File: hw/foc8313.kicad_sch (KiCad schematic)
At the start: 78 parts, among them J1 Tag Connect, J2 Encoder, J3 CAN, J4 CAN, J6 GPIO, SW1 SW_SPST, SW2 SW_SPST, U1 LMR36015SFBRNXR, U2 XC6206P332MR, U3 DRV8313PWP, U4 STM32F103CBTx, U5 AS5047D, X1 X322516MLB4SI

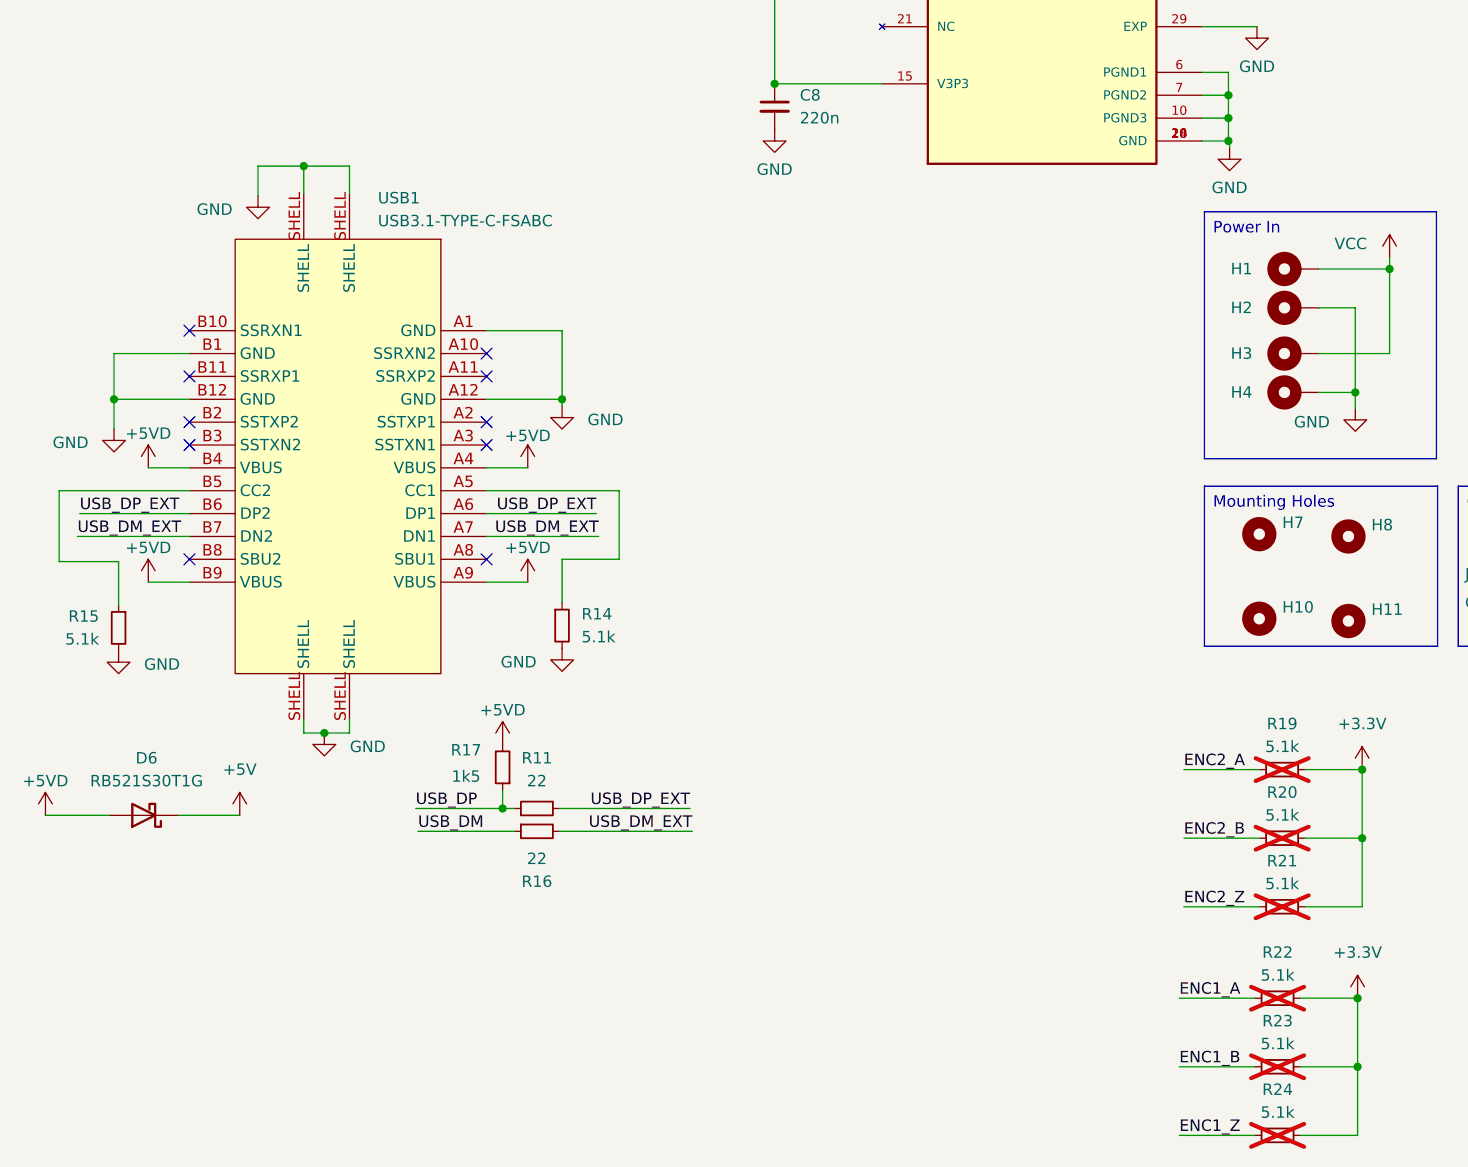
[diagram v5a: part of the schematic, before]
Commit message: [Hw]  LCSC versions of isolated CAN parts
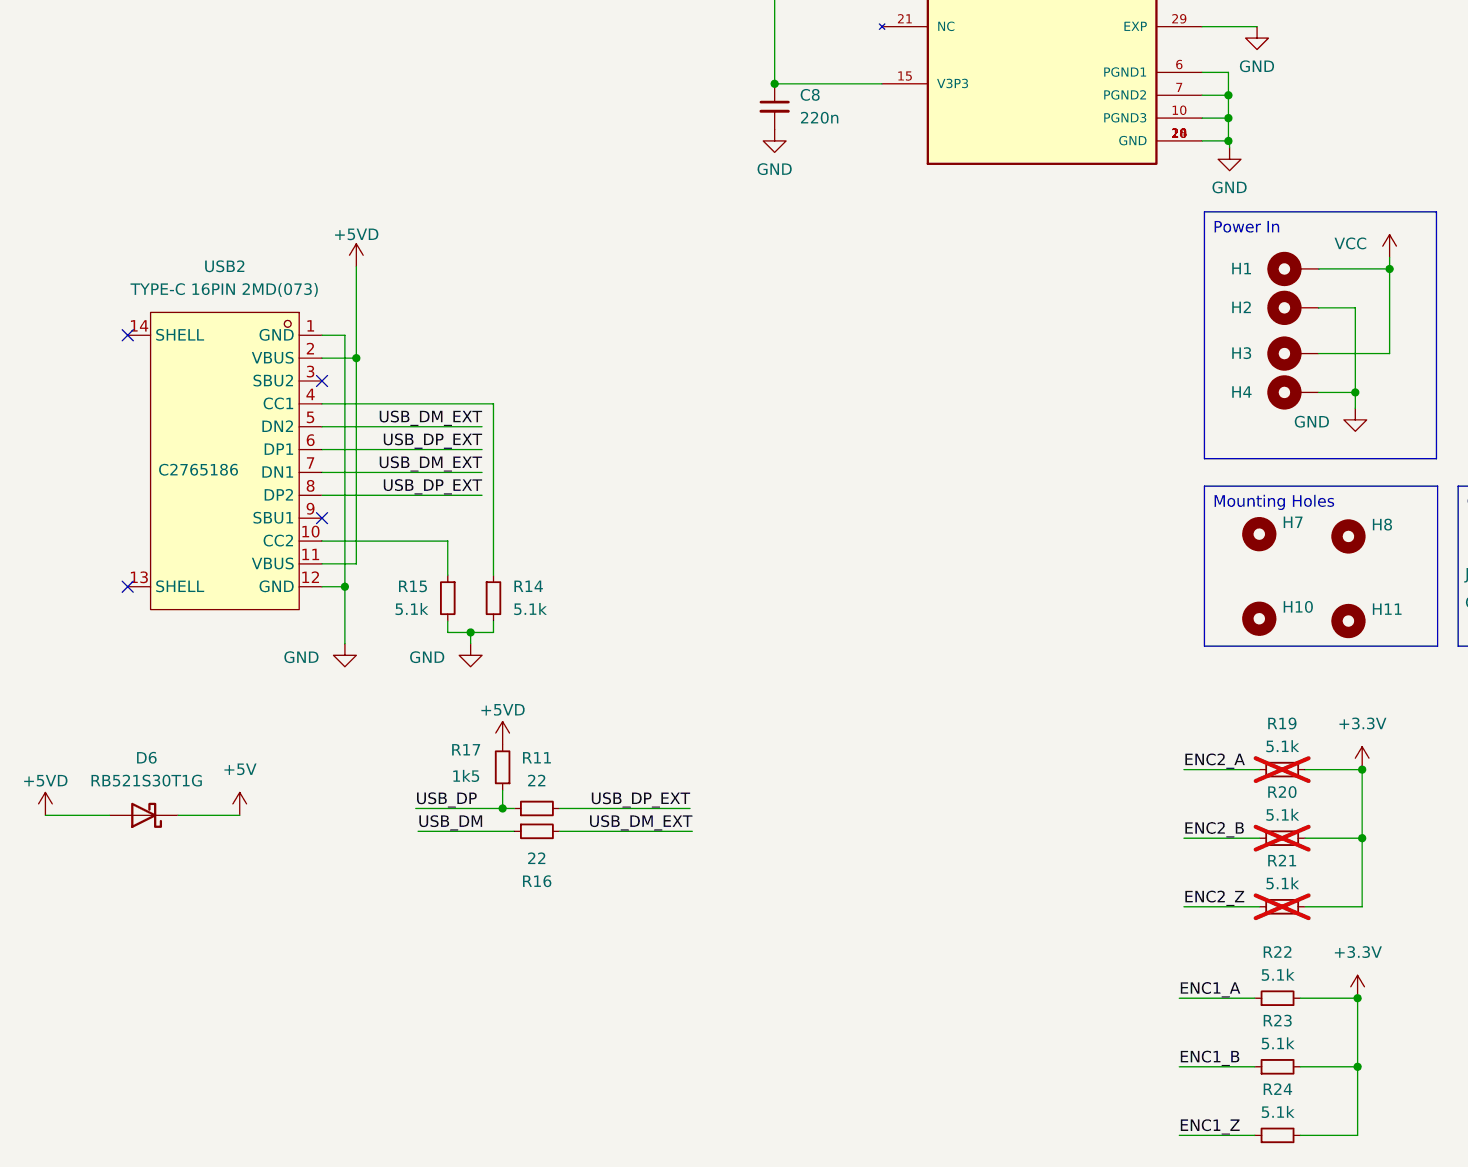
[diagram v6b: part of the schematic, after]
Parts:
- removed USB1: USB3.1-TYPE-C-FSABC, easyeda:USB-3.1-SMD_USB3.1-TYPE-C-FSABC, symbol easyeda:USB3.1-TYPE-C-FSABC
- added USB2: TYPE-C 16PIN 2MD(073), easyeda:USB-C-SMD_TYPE-C-6PIN-2MD-073, symbol easyeda:TYPE-C16PIN2MD(073)
- R22, R23, R24: now fitted
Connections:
- net +5VD: now also USB2.11 (VBUS), USB2.2 (VBUS)
- net GND: now also USB2.1 (GND), USB2.12 (GND)
- net USB_DM_EXT: now also USB2.5 (DN2), USB2.7 (DN1)
- net USB_DP_EXT: now also USB2.6 (DP1), USB2.8 (DP2)
- net at R14.1: now also USB2.4 (CC1)
- net at R15.1: now also USB2.10 (CC2)
- no-connect marks 19 -> 13
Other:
- moved on the sheet: R14, R15

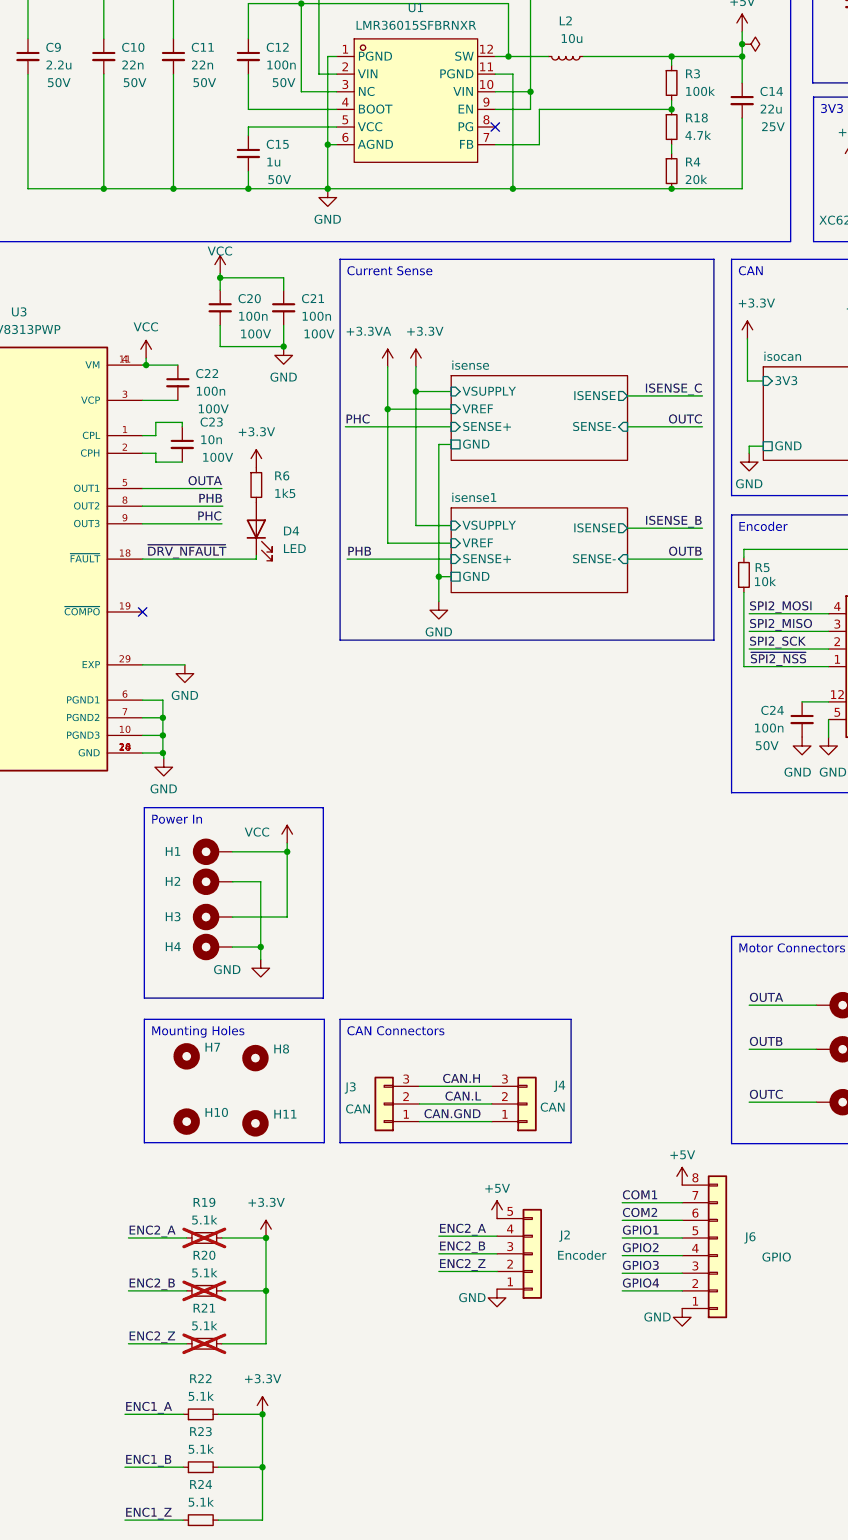
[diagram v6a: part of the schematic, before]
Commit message: [Hw] Rerouted for timer swap, usb replaced, hall pullups topside, silk version
Signed-off-by: Will Haarhoff <williamhaarhoff@gmail.com>
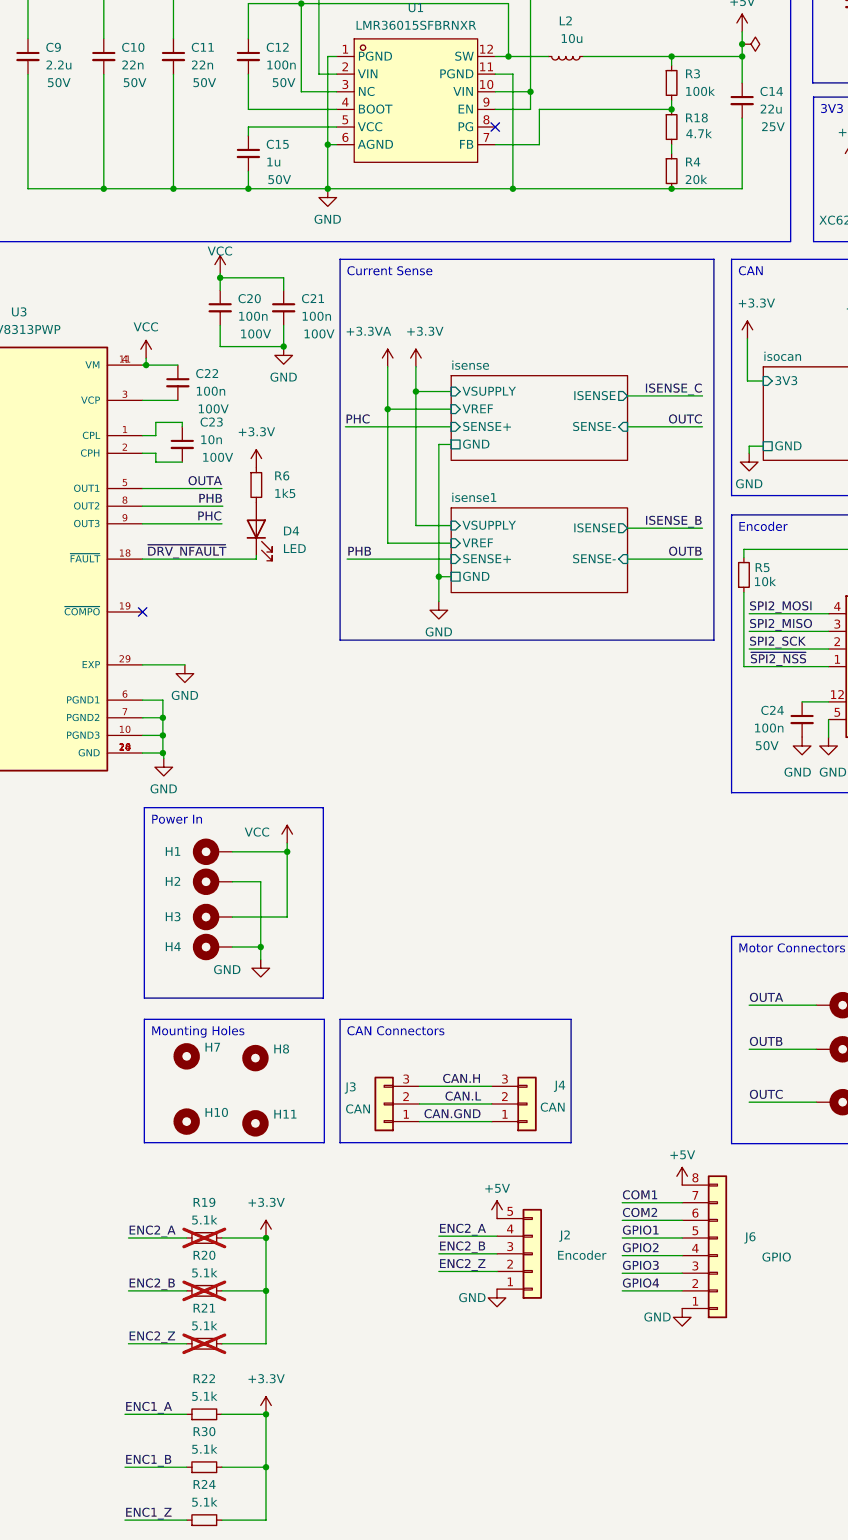
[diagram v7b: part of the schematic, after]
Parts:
- removed R23: 5.1k, Resistor_SMD:R_0402_1005Metric, symbol Device:R_Small
- added R30: 5.1k, Resistor_SMD:R_0402_1005Metric, symbol Device:R_Small
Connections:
- net +3.3V: now also R30.2
- net ENC1_B: now also R30.1

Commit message: [Hw] Cleaned up schematic, 10m isense shunts, green power led, DRC
Signed-off-by: Will Haarhoff <williamhaarhoff@gmail.com>
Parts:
- D7: value YELLOW -> GREEN; LCSC C72038 -> C2297
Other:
- moved on the sheet: C10, C11, C12, C14, C15, C16, C17, C18, C2, C20, C21, C22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
